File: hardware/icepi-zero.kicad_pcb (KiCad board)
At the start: 4 copper layers, 65 x 30 mm, 61 parts, among them J1 Micro_SD_Card_Det2, J2 Conn_02x20_Counter_Clockwise, J3 HDMI_C_1.3, J4 USB_C_Receptacle_USB2.0_14P, J5 USB_C_Receptacle_USB2.0_14P, J6 USB_C_Receptacle_USB2.0_14P, U1 ECP5U_12_CABGA256, U10 TPD2EUSB30A, U11 W25Q128JVS, U2 TLV62569DBV, U3 TLV62569DBV, U4 TLV62569DBV, U5 PCA9306DC1, U6 FT231XQ, U7 W9825G6KH, U8 TPD2EUSB30A, U9 TPD2EUSB30A

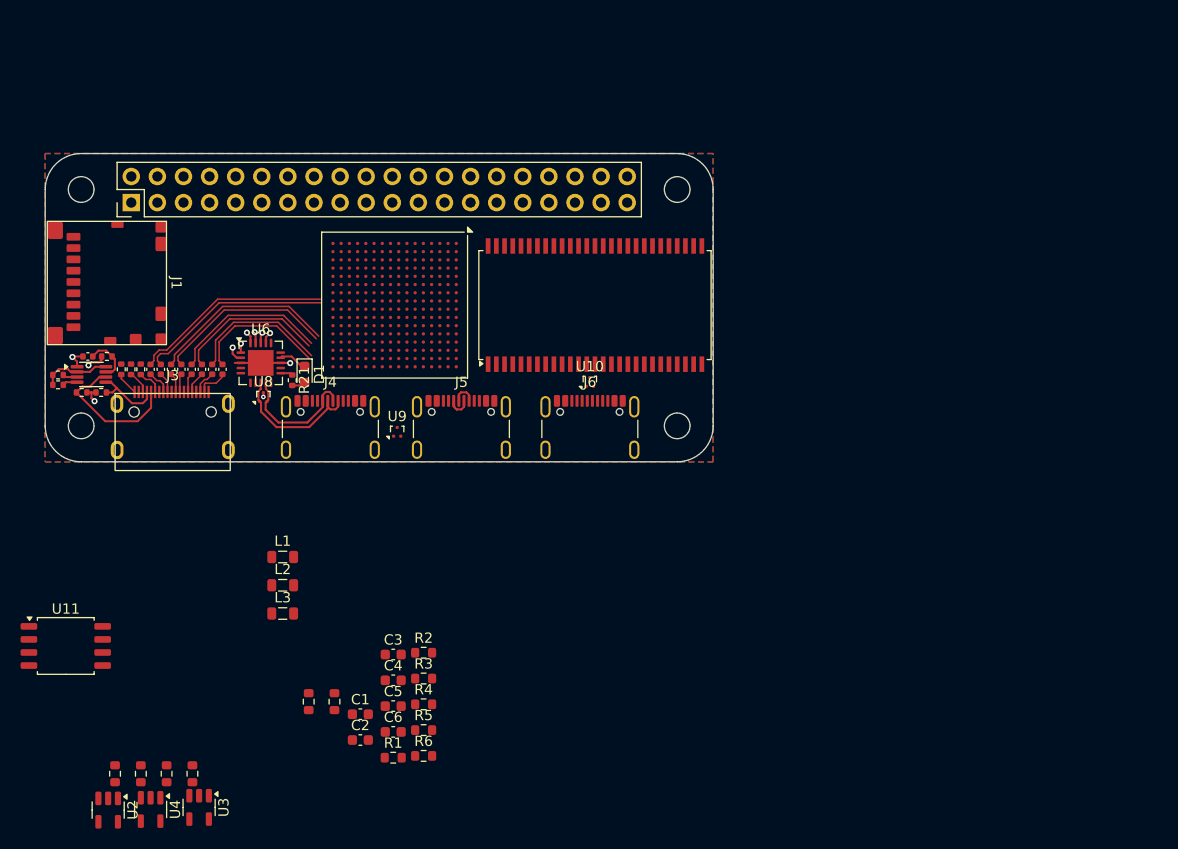
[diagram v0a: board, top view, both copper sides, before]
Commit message: Routed most of sdram
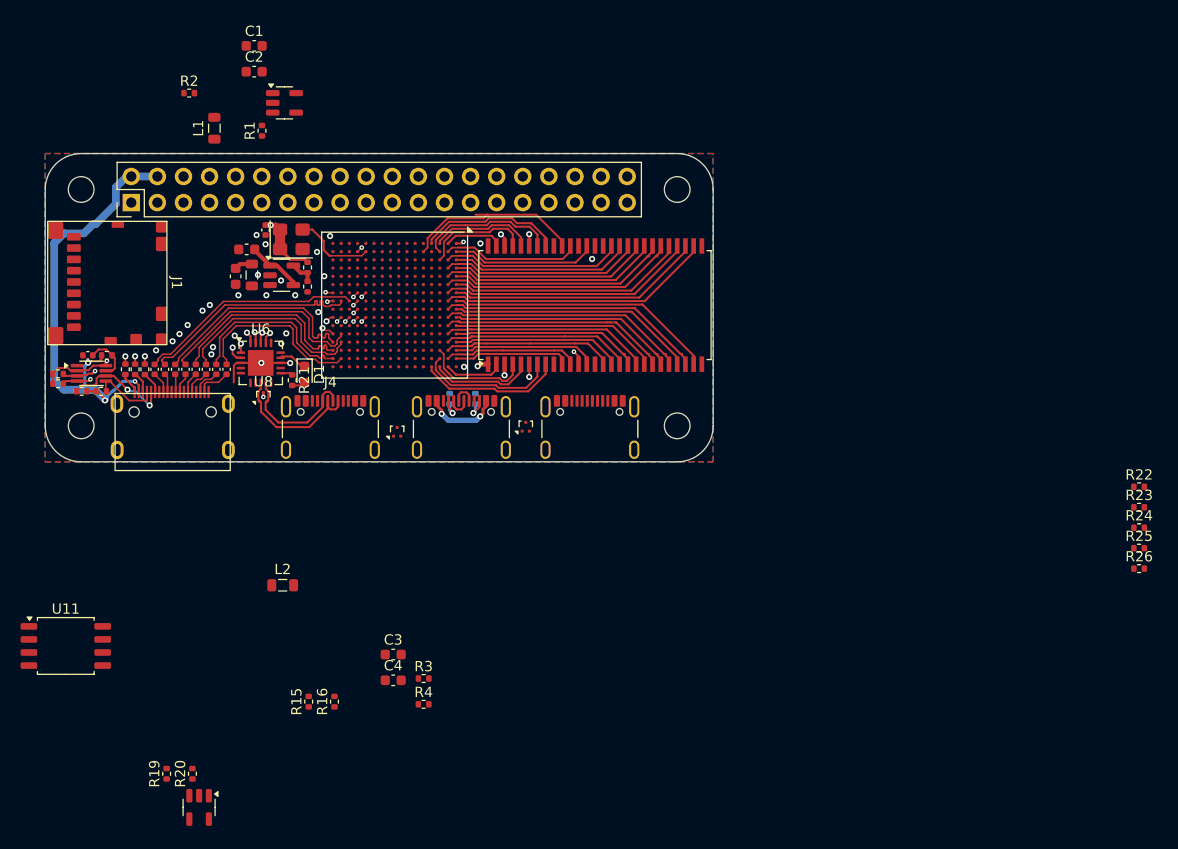
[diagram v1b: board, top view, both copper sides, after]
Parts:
- added C16: 100nF, Capacitor_SMD:C_0402_1005Metric, F.Cu at (137.4, 97.5)
- added R22: 4.7k, Resistor_SMD:R_0402_1005Metric, F.Cu at (222.4, 122.4)
- added R23: 10k, Resistor_SMD:R_0402_1005Metric, F.Cu at (222.4, 124.4)
- added R24: 10k, Resistor_SMD:R_0402_1005Metric, F.Cu at (222.4, 126.4)
- added R25: 10k, Resistor_SMD:R_0402_1005Metric, F.Cu at (222.4, 128.4)
- added R26: 10k, Resistor_SMD:R_0402_1005Metric, F.Cu at (222.4, 130.4)
- added Y1: YSO690PR, Oscillator:Oscillator_SMD_SiT_PQFN-4Pin_3.2x2.5mm, F.Cu at (139.9, 98.3)
- R1, R15, R16, R19, R2, R20, R3, R4, R5, R6: footprint Resistor_SMD:R_0603_1608Metric -> Resistor_SMD:R_0402_1005Metric
- R17, R18: footprint Resistor_SMD:R_0603_1608Metric -> Resistor_SMD:R_0402_1005Metric; moved to B.Cu
- moved U2 70.9 mm to (139.3, 85.1), turned to 0 degrees
- moved C1 65.9 mm to (136.3, 79.5)
- moved C2 65.9 mm to (136.3, 82.0)
- moved R1 62.3 mm to (137.1, 87.8), turned to 90 degrees
- moved R2 59.0 mm to (130.0, 84.1)
- moved U4 53.5 mm to (139.0, 101.8), turned to 0 degrees
- moved R17 48.9 mm to (155.4, 113.9)
- moved R18 48.9 mm to (157.9, 113.9), turned to -90 degrees
- moved R6 47.0 mm to (141.5, 103.0), turned to -90 degrees
- moved C6 46.9 mm to (134.5, 102.0), turned to -90 degrees
- moved C5 46.7 mm to (135.6, 99.3), turned to 180 degrees
- moved R5 46.4 mm to (141.5, 101.1), turned to -90 degrees
- moved L1 42.2 mm to (132.5, 87.5), turned to 90 degrees
- moved L3 33.1 mm to (136.1, 101.8), turned to 90 degrees
- moved U10 7.61 mm to (162.8, 116.6)
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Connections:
- net Net-(J3-CK+) renamed /GPIO/CONN_CK+
- net Net-(J3-CK-) renamed /GPIO/CONN_CK-
- net Net-(J3-D0+) renamed /GPIO/CONN_D0+
- net Net-(J3-D0-) renamed /GPIO/CONN_D0-
- net Net-(J3-D1+) renamed /GPIO/CONN_D1+
- net Net-(J3-D1-) renamed /GPIO/CONN_D1-
- net Net-(J3-D2+) renamed /GPIO/CONN_D2+
- net Net-(J3-D2-) renamed /GPIO/CONN_D2-
- net USB_TCK renamed JTAG_TCK
- net USB_TDI renamed JTAG_TDI
- net USB_TDO renamed JTAG_TDO
- net USB_TMS renamed JTAG_TMS
- C2 pad 2: Net-(U2-FB) -> GND
- C4 pad 2: Net-(U3-FB) -> GND
- C6 pad 2: Net-(U4-FB) -> GND
- U1 pad A10: unconnected-(U1C-PT42B/--PadA10) -> A10
- U1 pad A11: unconnected-(U1C-PT53A/+-PadA11) -> BA0
- U1 pad A12: unconnected-(U1C-PT53B/--PadA12) -> ~{RAS}
- U1 pad A13: unconnected-(U1C-PT65A/+-PadA13) -> ~{WE}
- U1 pad A14: unconnected-(U1C-PT65B/--PadA14) -> D7
- U1 pad A15: unconnected-(U1C-PT67B/--PadA15) -> D5
- U1 pad A2: unconnected-(U1B-PT4A/+-PadA2) -> D8
- U1 pad A3: unconnected-(U1B-PT6A/+-PadA3) -> CLK
- U1 pad A4: unconnected-(U1B-PT6B/--PadA4) -> A12
- U1 pad A5: unconnected-(U1B-PT18A/+-PadA5) -> A9
- U1 pad A6: unconnected-(U1B-PT18B/--PadA6) -> A7
- U1 pad A7: unconnected-(U1B-PT29A/+/PCLKT0_0-PadA7) -> A5
- U1 pad A8: unconnected-(U1B-PT29B/-/PCLKC0_0-PadA8) -> A3
- U1 pad A9: unconnected-(U1C-PT42A/+-PadA9) -> A1
- U1 pad B1: unconnected-(U1G-PL2A/+/HS/LDQ8-PadB1) -> D15
- U1 pad B10: unconnected-(U1C-PT44A/+-PadB10) -> A0
- U1 pad B11: unconnected-(U1C-PT49A/+-PadB11) -> BA1
- U1 pad B12: unconnected-(U1C-PT56A/+-PadB12) -> ~{CS}
- U1 pad B13: unconnected-(U1C-PT60A/+-PadB13) -> ~{CAS}
- U1 pad B14: unconnected-(U1C-PT67A/+-PadB14) -> DQM0
- U1 pad B15: unconnected-(U1D-PR2B/-/S0_IN/HS/RDQ8-PadB15) -> D6
- U1 pad B16: unconnected-(U1D-PR2A/+/HS/RDQ8-PadB16) -> D0
- U1 pad B2: unconnected-(U1G-PL2B/-/HS/LDQ8-PadB2) -> D9
- U1 pad B3: unconnected-(U1B-PT4B/--PadB3) -> DQM1
- U1 pad B4: unconnected-(U1B-PT11B/--PadB4) -> CKE
- U1 pad B5: unconnected-(U1B-PT15B/--PadB5) -> A11
- U1 pad B6: unconnected-(U1B-PT22B/--PadB6) -> A8
- U1 pad B7: unconnected-(U1B-PT27B/-/PCLKC0_1-PadB7) -> A6
- U1 pad B8: unconnected-(U1C-PT35B/-/PCLKC1_0-PadB8) -> A4
- U1 pad B9: unconnected-(U1C-PT38A/+/GR_PCLK1_0-PadB9) -> A2
- U1 pad C1: unconnected-(U1G-PL5A/+/HS/LDQ8-PadC1) -> D13
- U1 pad C14: unconnected-(U1D-PR2C/+/RDQ8-PadC14) -> D1
- U1 pad C15: unconnected-(U1D-PR5B/-/HS/RDQ8-PadC15) -> D3
- U1 pad C16: unconnected-(U1D-PR5A/+/HS/RDQ8-PadC16) -> D2
- U1 pad C2: unconnected-(U1G-PL5B/-/HS/LDQ8-PadC2) -> D12
- U1 pad C3: unconnected-(U1G-PL2C/+/LDQ8-PadC3) -> D14
- U1 pad D1: unconnected-(U1G-PL8A/+/HS/LDQS8-PadD1) -> D11
- U1 pad D16: unconnected-(U1D-PR8A/+/HS/RDQS8-PadD16) -> D4
- U1 pad E2: unconnected-(U1G-PL8B/-/HS/LDQSN8-PadE2) -> D10
- U1 pad M2: unconnected-(U1F-PL26D/-/PCLKC6_0/LDQ32-PadM2) -> GLOBAL_CLK
- U1 pad M7: unconnected-(U1H-PB9B/-/D2/IO2-PadM7) -> ~{FLASH_WP}
- U1 pad N10: unconnected-(U1H-CFG_0-PadN10) -> GND
- U1 pad N7: unconnected-(U1H-PB9A/+/D3/IO3-PadN7) -> ~{FLASH_RESET}
- U1 pad N8: unconnected-(U1H-PB15A/+/HOLDN/DI/BUSY/CSSPIN/CEN-PadN8) -> ~{FLASH_CS}
- U1 pad N9: unconnected-(U1H-CCLK/MCLK/SCK-PadN9) -> FLASH_CLK
- U1 pad P10: unconnected-(U1H-CFG_1-PadP10) -> +3V3
- U1 pad P8: unconnected-(U1H-PB13B/-/CS1N-PadP8) -> FPDI_CLK-
- U1 pad R10: unconnected-(U1H-CFG_2-PadR10) -> GND
- U1 pad R12: unconnected-(U1E-PR44A/+/HS/RDQS44-PadR12) -> FPDI_D0+
- U1 pad R13: unconnected-(U1E-PR41C/+/RDQ44-PadR13) -> FPDI_D1+
- U1 pad R15: unconnected-(U1E-PR38C/+/RDQ44-PadR15) -> FPDI_D2+
- U1 pad R8: unconnected-(U1H-PB13A/+/SN/CSN-PadR8) -> FPDI_CLK+
- U1 pad T13: unconnected-(U1E-PR44B/-/HS/RDQSN44-PadT13) -> FPDI_D0-
- U1 pad T14: unconnected-(U1E-PR41D/-/RDQ44-PadT14) -> FPDI_D1-
- U1 pad T15: unconnected-(U1E-PR38D/-/RDQ44-PadT15) -> FPDI_D2-
- U1 pad T7: unconnected-(U1H-PB11A/+/D1/MISO/IO1-PadT7) -> FLASH_MISO
- U1 pad T8: unconnected-(U1H-PB11B/-/D0/MOSI/IO0-PadT8) -> FLASH_MOSI
- U11 pad 1: unconnected-(U11-~{CS}-Pad1) -> ~{FLASH_CS}
- U11 pad 2: unconnected-(U11-DO/IO_{1}-Pad2) -> FLASH_MISO
- U11 pad 3: unconnected-(U11-~{WP}/IO_{2}-Pad3) -> ~{FLASH_WP}
- U11 pad 5: unconnected-(U11-DI/IO_{0}-Pad5) -> FLASH_MOSI
- U11 pad 6: unconnected-(U11-CLK-Pad6) -> FLASH_CLK
- U11 pad 7: unconnected-(U11-~{HOLD}/~{RESET}/IO_{3}-Pad7) -> ~{FLASH_RESET}
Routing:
- net +5V: track 7.41 -> 57.6 mm, vias 2 -> 5
- net A4: track 0.00 -> 26.7 mm
- net A2: track 0.00 -> 26.1 mm
- net A3: track 0.00 -> 26.1 mm
- net A6: track 0.00 -> 24.9 mm
- net A5: track 0.00 -> 24.9 mm
- net A0: track 0.00 -> 24.1 mm
- net A1: track 0.00 -> 24.1 mm
- net A8: track 0.00 -> 23.2 mm
- net A7: track 0.00 -> 23.1 mm
- net A10: track 0.00 -> 22.2 mm
- net BA1: track 0.00 -> 22.2 mm
- net A9: track 0.00 -> 21.3 mm
- net A11: track 0.00 -> 21.2 mm
- net BA0: track 0.00 -> 20.2 mm
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
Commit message: Routed power
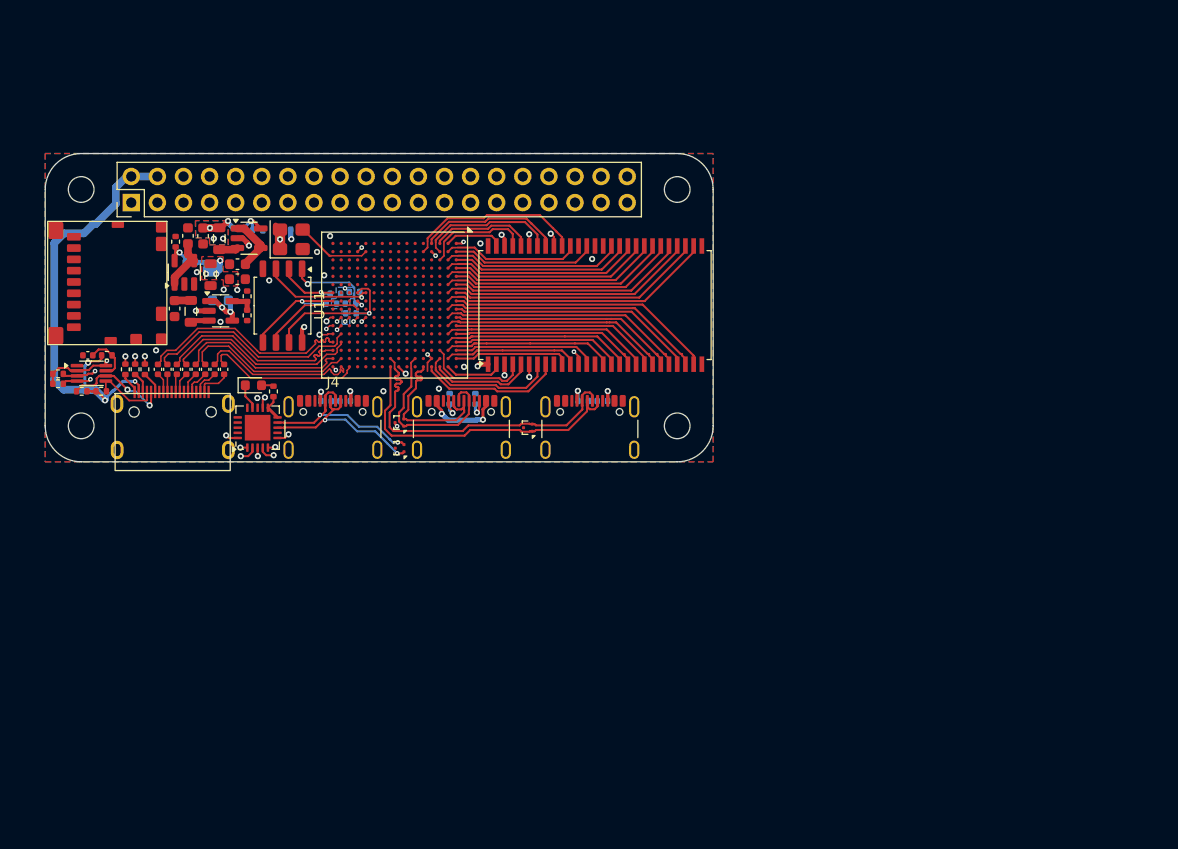
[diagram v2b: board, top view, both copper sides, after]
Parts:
- C16, C3, R1, R15, R16, R19, R20, R22, R23, R24, R25, R26, R5, R6: moved to B.Cu
- moved R24 81.6 mm to (143.8, 104.6), turned to 180 degrees
- moved R26 81.0 mm to (146.1, 103.5)
- moved R23 80.9 mm to (144.2, 103.7), turned to 180 degrees
- moved R25 80.0 mm to (145.8, 105.5)
- moved R22 78.8 mm to (145.7, 104.6)
- moved R19 54.4 mm to (168.4, 114.1), turned to 0 degrees
- moved R20 53.9 mm to (170.2, 114.1), turned to 0 degrees
- moved U3 48.4 mm to (133.1, 105.3), turned to 0 degrees
- moved R4 43.3 mm to (135.7, 103.9), turned to 90 degrees
- moved C4 42.0 mm to (128.6, 105.1), turned to -90 degrees
- moved R3 39.3 mm to (135.7, 105.8), turned to 90 degrees
- moved U11 39.3 mm to (139.1, 104.8), turned to -90 degrees
- moved C3 38.3 mm to (133.1, 104.3), turned to 180 degrees
- moved R15 29.3 mm to (143.3, 114.1), turned to 0 degrees
- moved R16 29.3 mm to (145.2, 114.1), turned to 0 degrees
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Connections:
- U1 pad E16: unconnected-(U1D-PR11D/-/RDQ8-PadE16) -> D2-
- U1 pad F15: unconnected-(U1D-PR11C/+/RDQ8-PadF15) -> D2+
- U1 pad J15: unconnected-(U1D-PR23B/-/PCLKC2_1/HS/RDQ20-PadJ15) -> D3-
- U1 pad J16: unconnected-(U1D-PR23A/+/PCLKT2_1/HS/RDQ20-PadJ16) -> D3+
- U1 pad P16: unconnected-(U1E-PR35A/+/HS/RDQ32-PadP16) -> FPDI_D2+
- U1 pad P8: FPDI_CLK- -> unconnected-(U1H-PB13B/-/CS1N-PadP8)
- U1 pad R12: FPDI_D0+ -> FPDI_CLK+
- U1 pad R13: FPDI_D1+ -> FPDI_D0+
- U1 pad R15: FPDI_D2+ -> FPDI_D1+
- U1 pad R16: unconnected-(U1E-PR35B/-/VREF1_3/HS/RDQ32-PadR16) -> FPDI_D2-
- U1 pad R8: FPDI_CLK+ -> unconnected-(U1H-PB13A/+/SN/CSN-PadR8)
- U1 pad T13: FPDI_D0- -> FPDI_CLK-
- U1 pad T14: FPDI_D1- -> FPDI_D0-
- U1 pad T15: FPDI_D2- -> FPDI_D1-
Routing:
- net D3-: track 0.00 -> 32.0 mm
- net D3+: track 0.00 -> 30.7 mm
- net D2+: track 2.38 -> 17.9 mm
- net D2-: track 2.34 -> 16.7 mm
- net ~{FLASH_RESET}: track 0.58 -> 14.7 mm
- net +5V: track 57.6 -> 68.9 mm, vias 5 -> 8
- net FLASH_MOSI: track 0.59 -> 11.4 mm
- net ~{FLASH_WP}: track 0.57 -> 10.9 mm
- net +1V1: track 0.00 -> 10.2 mm, vias 0 -> 3
- net FLASH_CLK: track 0.54 -> 10.1 mm, vias 1 -> 0
- net ~{FLASH_CS}: track 0.58 -> 9.35 mm, vias 1 -> 2
- net D1-: track 12.5 -> 18.9 mm, vias 0 -> 2
- net FLASH_MISO: track 0.74 -> 6.68 mm
- net D1+: track 14.0 -> 17.8 mm, vias 0 -> 2
- net Net-(U2-FB): track 0.00 -> 2.96 mm, vias 0 -> 1
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- added copper zone on F.Cu, net +1V1
- added copper zone on B.Cu, net +3V3
- added copper zone on F.Cu, net +3V3
